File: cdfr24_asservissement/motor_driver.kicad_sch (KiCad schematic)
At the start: 14 parts

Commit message: Place components
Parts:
- renumbered C26 to C19, CR1 to CR2, C27 to Cen2, R11 to R14, R21 to R15, R22 to R16
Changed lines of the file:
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@@
 		(dnp no)
 		(fields_autoplaced yes)
-		(property "Reference" "#PWR022"
+		(property "Reference" "#PWR067"
 			(at 233.68 68.58 0)
 			(effects
@@
 			(project "cdfr24_asservissement"
 				(path "/c6b82269-16f5-49e6-8b51-4d12a40a3077/084e419c-7880-44c5-a0d2-721d5e789f19"
-					(reference "#PWR022")
-					(unit 1)
-				)
-				(path "/c6b82269-16f5-49e6-8b51-4d12a40a3077/fbaa2c7d-8eee-479f-b1be-bb54414743c2"
-					(reference "#PWR016")
+					(reference "#PWR067")
+					(unit 1)
+				)
+				(path "/c6b82269-16f5-49e6-8b51-4d12a40a3077/fbaa2c7d-8eee-479f-b1be-bb54414743c2"
+					(reference "#PWR058")
 					(unit 1)
 				)
@@
 		(dnp no)
 		(fields_autoplaced yes)
-		(property "Reference" "#PWR052"
+		(property "Reference" "#PWR070"
 			(at 194.31 100.33 0)
 			(effects
@@
 			(project "cdfr24_asservissement"
 				(path "/c6b82269-16f5-49e6-8b51-4d12a40a3077/084e419c-7880-44c5-a0d2-721d5e789f19"
-					(reference "#PWR052")
-					(unit 1)
-				)
-				(path "/c6b82269-16f5-49e6-8b51-4d12a40a3077/fbaa2c7d-8eee-479f-b1be-bb54414743c2"
-					(reference "#PWR046")
+					(reference "#PWR070")
+					(unit 1)
+				)
+				(path "/c6b82269-16f5-49e6-8b51-4d12a40a3077/fbaa2c7d-8eee-479f-b1be-bb54414743c2"
+					(reference "#PWR061")
 					(unit 1)
 				)
@@
 		(dnp no)
 		(fields_autoplaced yes)
-		(property "Reference" "#PWR057"
+		(property "Reference" "#PWR068"
 			(at 107.95 93.98 0)
 			(effects
@@
 			(project "cdfr24_asservissement"
 				(path "/c6b82269-16f5-49e6-8b51-4d12a40a3077/084e419c-7880-44c5-a0d2-721d5e789f19"
-					(reference "#PWR057")
-					(unit 1)
-				)
-				(path "/c6b82269-16f5-49e6-8b51-4d12a40a3077/fbaa2c7d-8eee-479f-b1be-bb54414743c2"
-					(reference "#PWR044")
+					(reference "#PWR068")
+					(unit 1)
+				)
+				(path "/c6b82269-16f5-49e6-8b51-4d12a40a3077/fbaa2c7d-8eee-479f-b1be-bb54414743c2"
+					(reference "#PWR059")
 					(unit 1)
 				)
@@
 		(on_board yes)
 		(dnp no)
-		(property "Reference" "R21"
+		(property "Reference" "R15"
 			(at 124.46 96.647 90)
 			(effects
@@
 			(project "cdfr24_asservissement"
 				(path "/c6b82269-16f5-49e6-8b51-4d12a40a3077/084e419c-7880-44c5-a0d2-721d5e789f19"
-					(reference "R21")
+					(reference "R15")
 					(unit 1)
 				)
@@
 		(dnp no)
 		(fields_autoplaced yes)
-		(property "Reference" "R22"
+		(property "Reference" "R16"
 			(at 197.104 102.87 0)
 			(effects
@@
 			(project "cdfr24_asservissement"
 				(path "/c6b82269-16f5-49e6-8b51-4d12a40a3077/084e419c-7880-44c5-a0d2-721d5e789f19"
-					(reference "R22")
-					(unit 1)
-				)
-				(path "/c6b82269-16f5-49e6-8b51-4d12a40a3077/fbaa2c7d-8eee-479f-b1be-bb54414743c2"
-					(reference "R20")
+					(reference "R16")
+					(unit 1)
+				)
+				(path "/c6b82269-16f5-49e6-8b51-4d12a40a3077/fbaa2c7d-8eee-479f-b1be-bb54414743c2"
+					(reference "R13")
 					(unit 1)
 				)
@@
 		(on_board yes)
 		(dnp no)
-		(property "Reference" "#PWR058"
+		(property "Reference" "#PWR069"
 			(at 124.46 83.82 0)
 			(effects
@@
 			(project "cdfr24_asservissement"
 				(path "/c6b82269-16f5-49e6-8b51-4d12a40a3077/084e419c-7880-44c5-a0d2-721d5e789f19"
-					(reference "#PWR058")
-					(unit 1)
-				)
-				(path "/c6b82269-16f5-49e6-8b51-4d12a40a3077/fbaa2c7d-8eee-479f-b1be-bb54414743c2"
-					(reference "#PWR045")
+					(reference "#PWR069")
+					(unit 1)
+				)
+				(path "/c6b82269-16f5-49e6-8b51-4d12a40a3077/fbaa2c7d-8eee-479f-b1be-bb54414743c2"
+					(reference "#PWR060")
 					(unit 1)
 				)
@@
 		(dnp no)
 		(fields_autoplaced yes)
-		(property "Reference" "R11"
+		(property "Reference" "R14"
 			(at 231.14 26.67 90)
 			(effects
@@
 			(project "cdfr24_asservissement"
 				(path "/c6b82269-16f5-49e6-8b51-4d12a40a3077/084e419c-7880-44c5-a0d2-721d5e789f19"
-					(reference "R11")
+					(reference "R14")
 					(unit 1)
 				)
@@
 		(dnp no)
 		(fields_autoplaced yes)
-		(property "Reference" "#PWR064"
+		(property "Reference" "#PWR073"
 			(at 82.55 153.67 0)
 			(effects
@@
 			(project "cdfr24_asservissement"
 				(path "/c6b82269-16f5-49e6-8b51-4d12a40a3077/084e419c-7880-44c5-a0d2-721d5e789f19"
+					(reference "#PWR073")
+					(unit 1)
+				)
+				(path "/c6b82269-16f5-49e6-8b51-4d12a40a3077/fbaa2c7d-8eee-479f-b1be-bb54414743c2"
 					(reference "#PWR064")
-					(unit 1)
-				)
-				(path "/c6b82269-16f5-49e6-8b51-4d12a40a3077/fbaa2c7d-8eee-479f-b1be-bb54414743c2"
-					(reference "#PWR049")
 					(unit 1)
 				)
@@
 		(dnp no)
 		(fields_autoplaced yes)
-		(property "Reference" "#PWR028"
+		(property "Reference" "#PWR065"
 			(at 224.79 38.1 0)
 			(effects
@@
 			(project "cdfr24_asservissement"
 				(path "/c6b82269-16f5-49e6-8b51-4d12a40a3077/084e419c-7880-44c5-a0d2-721d5e789f19"
-					(reference "#PWR028")
-					(unit 1)
-				)
-				(path "/c6b82269-16f5-49e6-8b51-4d12a40a3077/fbaa2c7d-8eee-479f-b1be-bb54414743c2"
-					(reference "#PWR025")
+					(reference "#PWR065")
+					(unit 1)
+				)
+				(path "/c6b82269-16f5-49e6-8b51-4d12a40a3077/fbaa2c7d-8eee-479f-b1be-bb54414743c2"
+					(reference "#PWR056")
 					(unit 1)
 				)
@@
 		(dnp no)
 		(fields_autoplaced yes)
-		(property "Reference" "CR1"
+		(property "Reference" "CR2"
 			(at 154.94 90.17 0)
 			(effects
@@
 		(dnp no)
 		(fields_autoplaced yes)
-		(property "Reference" "#PWR060"
+		(property "Reference" "#PWR071"
 			(at 97.79 114.3 0)
 			(effects
@@
 			(project "cdfr24_asservissement"
 				(path "/c6b82269-16f5-49e6-8b51-4d12a40a3077/084e419c-7880-44c5-a0d2-721d5e789f19"
-					(reference "#PWR060")
-					(unit 1)
-				)
-				(path "/c6b82269-16f5-49e6-8b51-4d12a40a3077/fbaa2c7d-8eee-479f-b1be-bb54414743c2"
-					(reference "#PWR047")
+					(reference "#PWR071")
+					(unit 1)
+				)
+				(path "/c6b82269-16f5-49e6-8b51-4d12a40a3077/fbaa2c7d-8eee-479f-b1be-bb54414743c2"
+					(reference "#PWR062")
 					(unit 1)
 				)
@@
 		(dnp no)
 		(fields_autoplaced yes)
-		(property "Reference" "C27"
-			(at 116.84 78.232 90)
+		(property "Reference" "Cen2"
+			(at 116.84 77.47 90)
 			(effects
 				(font
@@
 		)
 		(property "Value" "5.6n"
-			(at 116.84 80.772 90)
+			(at 116.84 80.01 90)
 			(effects
 				(font
@@
 			(project "cdfr24_asservissement"
 				(path "/c6b82269-16f5-49e6-8b51-4d12a40a3077/084e419c-7880-44c5-a0d2-721d5e789f19"
-					(reference "C27")
+					(reference "Cen2")
 					(unit 1)
 				)
@@
 		(dnp no)
 		(fields_autoplaced yes)
-		(property "Reference" "#PWR063"
+		(property "Reference" "#PWR072"
 			(at 82.55 137.16 0)
 			(effects
@@
 			(project "cdfr24_asservissement"
 				(path "/c6b82269-16f5-49e6-8b51-4d12a40a3077/084e419c-7880-44c5-a0d2-721d5e789f19"
+					(reference "#PWR072")
+					(unit 1)
+				)
+				(path "/c6b82269-16f5-49e6-8b51-4d12a40a3077/fbaa2c7d-8eee-479f-b1be-bb54414743c2"
 					(reference "#PWR063")
-					(unit 1)
-				)
-				(path "/c6b82269-16f5-49e6-8b51-4d12a40a3077/fbaa2c7d-8eee-479f-b1be-bb54414743c2"
-					(reference "#PWR048")
 					(unit 1)
 				)
@@
 		(dnp no)
 		(fields_autoplaced yes)
-		(property "Reference" "C26"
+		(property "Reference" "C19"
 			(at 221.996 53.34 0)
 			(effects
@@
 			(project "cdfr24_asservissement"
 				(path "/c6b82269-16f5-49e6-8b51-4d12a40a3077/084e419c-7880-44c5-a0d2-721d5e789f19"
-					(reference "C26")
-					(unit 1)
-				)
-				(path "/c6b82269-16f5-49e6-8b51-4d12a40a3077/fbaa2c7d-8eee-479f-b1be-bb54414743c2"
 					(reference "C19")
+					(unit 1)
+				)
+				(path "/c6b82269-16f5-49e6-8b51-4d12a40a3077/fbaa2c7d-8eee-479f-b1be-bb54414743c2"
+					(reference "C18")
 					(unit 1)
 				)
@@
 		(dnp no)
 		(fields_autoplaced yes)
-		(property "Reference" "#PWR055"
+		(property "Reference" "#PWR066"
 			(at 218.44 66.04 0)
 			(effects
@@
 			(project "cdfr24_asservissement"
 				(path "/c6b82269-16f5-49e6-8b51-4d12a40a3077/084e419c-7880-44c5-a0d2-721d5e789f19"
-					(reference "#PWR055")
-					(unit 1)
-				)
-				(path "/c6b82269-16f5-49e6-8b51-4d12a40a3077/fbaa2c7d-8eee-479f-b1be-bb54414743c2"
-					(reference "#PWR042")
+					(reference "#PWR066")
+					(unit 1)
+				)
+				(path "/c6b82269-16f5-49e6-8b51-4d12a40a3077/fbaa2c7d-8eee-479f-b1be-bb54414743c2"
+					(reference "#PWR057")
 					(unit 1)
 				)
@@
 		(dnp no)
 		(fields_autoplaced yes)
-		(property "Reference" "CR1"
+		(property "Reference" "CR2"
 			(at 274.32 52.0699 0)
 			(effects

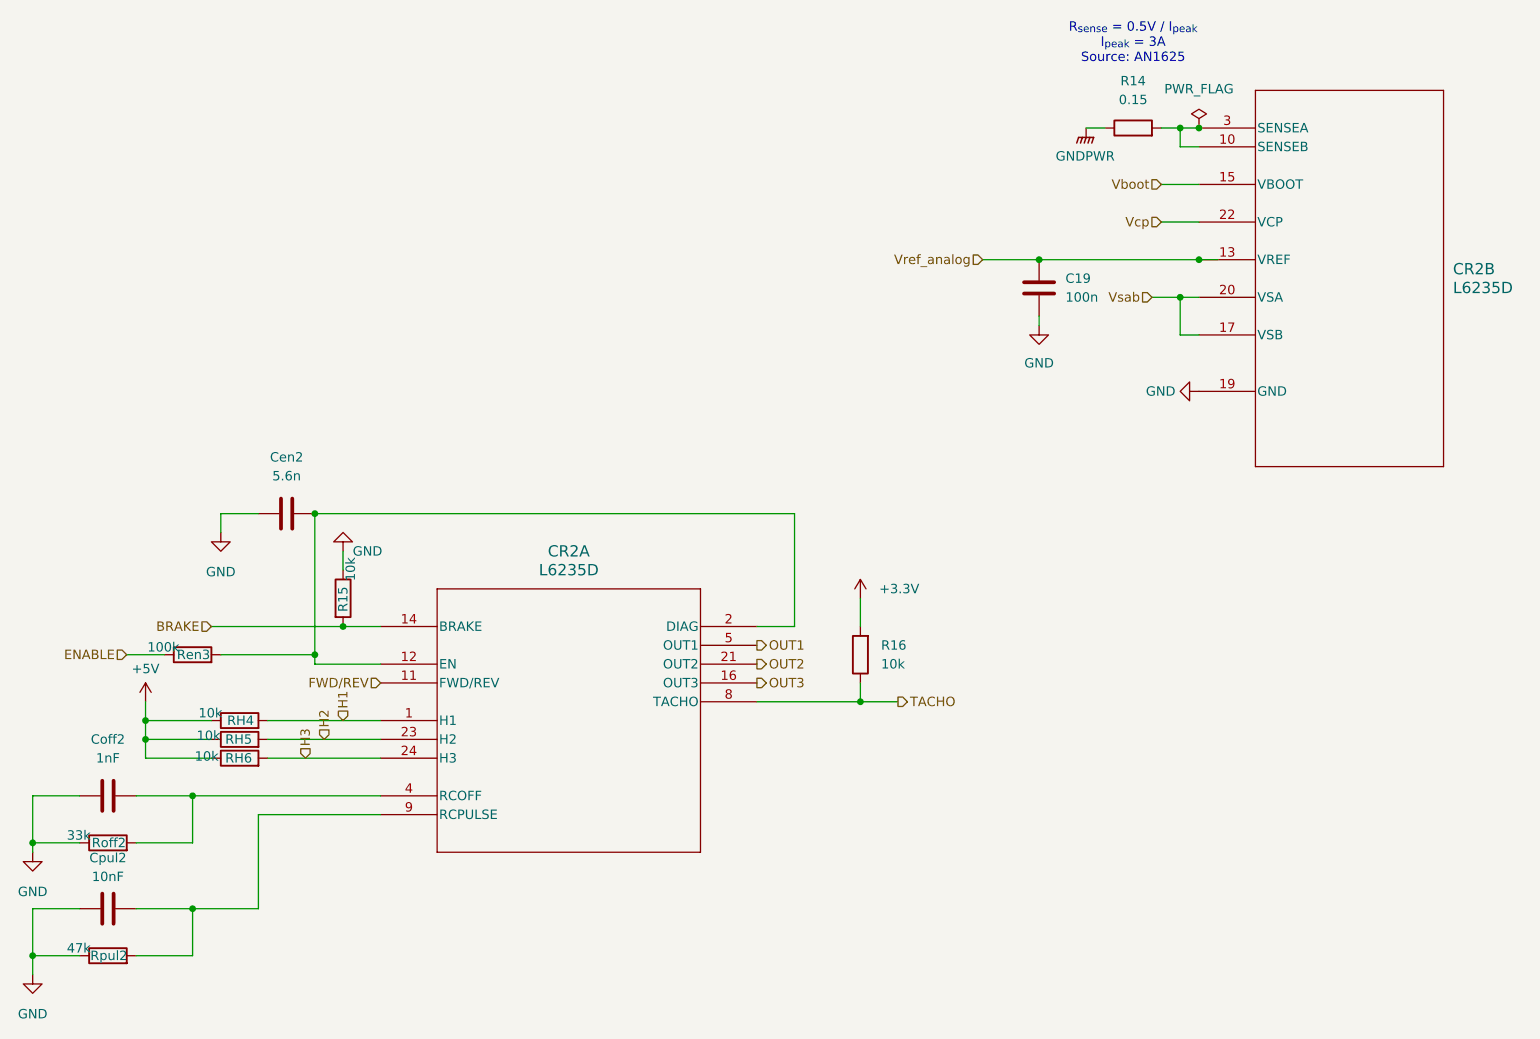
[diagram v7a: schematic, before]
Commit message: Improve placement
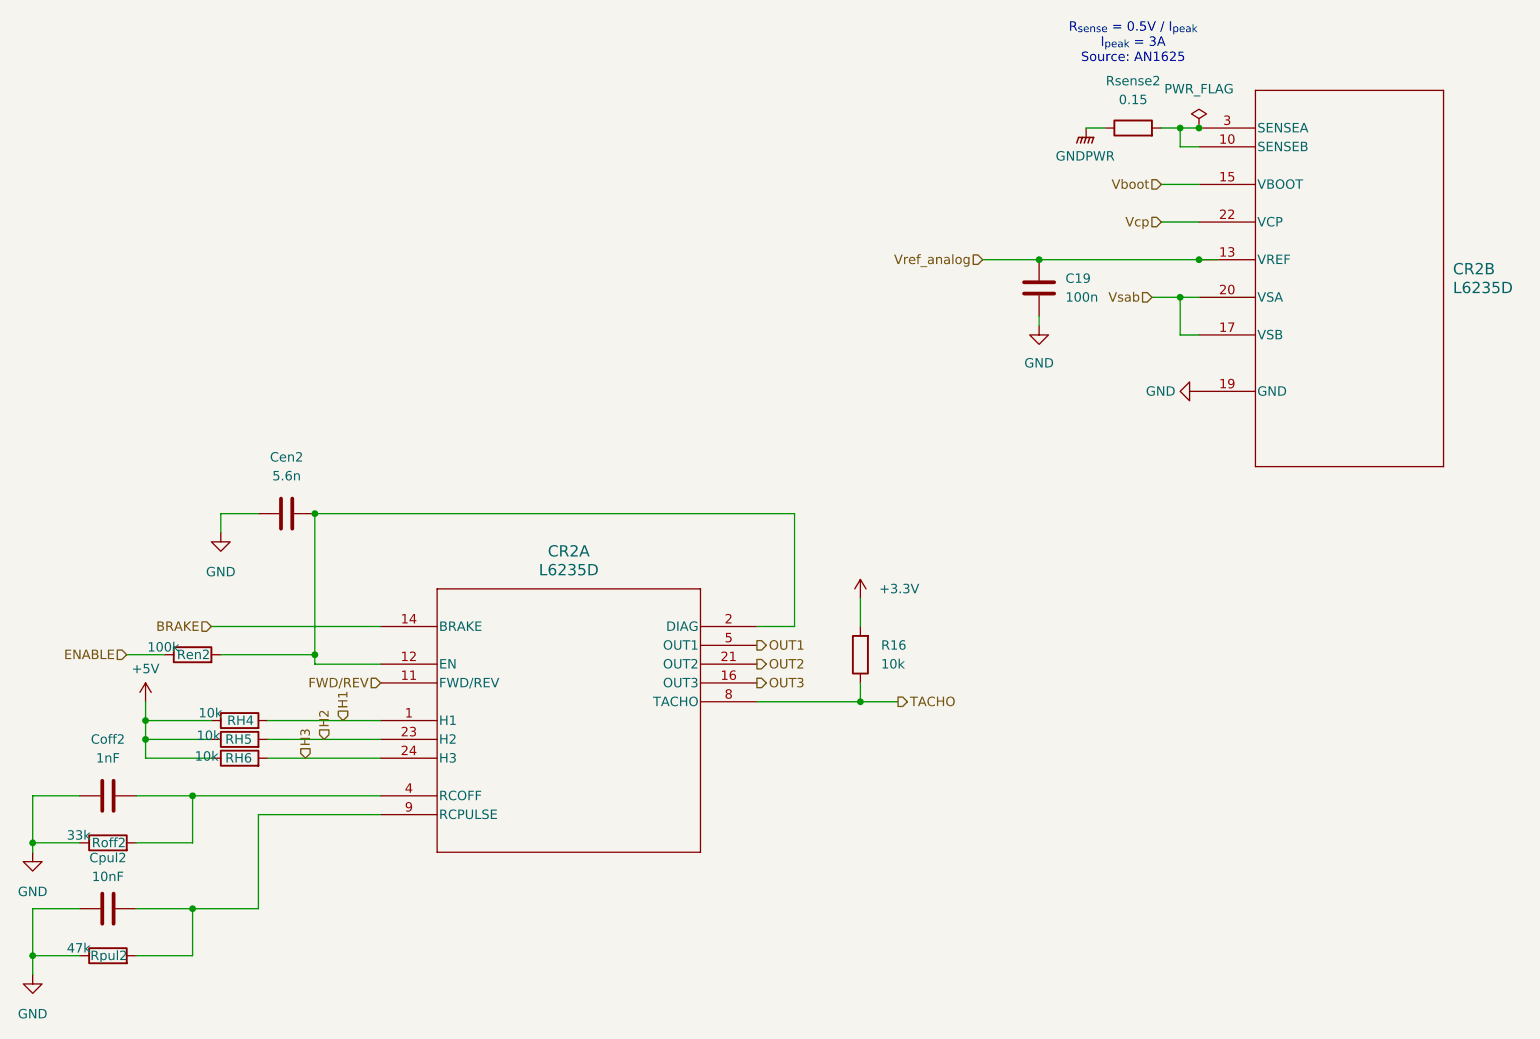
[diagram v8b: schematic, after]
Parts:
- removed R15: 10k, Resistor_SMD:R_0805_2012Metric_Pad1.20x1.40mm_HandSolder, symbol Device:R
- renumbered Ren3 to Ren2, R14 to Rsense2
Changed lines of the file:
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@@
-	)
-	(junction
-		(at 124.46 100.33)
-		(diameter 0)
-		(color 0 0 0 0)
 	)
 	(junction
@@
 	(wire
 		(pts
-			(xy 129.54 100.33) (xy 124.46 100.33)
+			(xy 106.68 100.33) (xy 129.54 100.33)
 		)
 		(stroke
@@
 	(wire
 		(pts
-			(xy 106.68 100.33) (xy 124.46 100.33)
-		)
-		(stroke
-			(width 0)
-			(type default)
-		)
-	)
-	(wire
-		(pts
 			(xy 234.95 40.64) (xy 240.03 40.64)
 		)
@@
 		(pts
 			(xy 218.44 58.42) (xy 218.44 59.69)
-		)
-		(stroke
-			(width 0)
-			(type default)
-		)
-	)
-	(wire
-		(pts
-			(xy 124.46 90.17) (xy 124.46 92.71)
 		)
 		(stroke
@@
 				)
 				(path "/c6b82269-16f5-49e6-8b51-4d12a40a3077/fbaa2c7d-8eee-479f-b1be-bb54414743c2"
-					(reference "#PWR058")
+					(reference "#PWR059")
 					(unit 1)
 				)
@@
 		(dnp no)
 		(fields_autoplaced yes)
-		(property "Reference" "#PWR070"
+		(property "Reference" "#PWR069"
 			(at 194.31 100.33 0)
 			(effects
@@
 			(project "cdfr24_asservissement"
 				(path "/c6b82269-16f5-49e6-8b51-4d12a40a3077/084e419c-7880-44c5-a0d2-721d5e789f19"
-					(reference "#PWR070")
+					(reference "#PWR069")
 					(unit 1)
 				)
@@
 				)
 				(path "/c6b82269-16f5-49e6-8b51-4d12a40a3077/fbaa2c7d-8eee-479f-b1be-bb54414743c2"
-					(reference "#PWR059")
-					(unit 1)
-				)
-			)
-		)
-	)
-	(symbol
-		(lib_id "Device:R")
-		(at 124.46 96.52 0)
-		(unit 1)
-		(exclude_from_sim no)
-		(in_bom yes)
-		(on_board yes)
-		(dnp no)
-		(property "Reference" "R15"
-			(at 124.46 96.647 90)
-			(effects
-				(font
-					(size 1.27 1.27)
-				)
-			)
-		)
-		(property "Value" "10k"
-			(at 125.476 92.583 90)
-			(effects
-				(font
-					(size 1.27 1.27)
-				)
-			)
-		)
-		(property "Footprint" "Resistor_SMD:R_0805_2012Metric_Pad1.20x1.40mm_HandSolder"
-			(at 122.682 96.52 90)
-			(effects
-				(font
-					(size 1.27 1.27)
-				)
-				(hide yes)
-			)
-		)
-		(property "Datasheet" "~"
-			(at 124.46 96.52 0)
-			(effects
-				(font
-					(size 1.27 1.27)
-				)
-				(hide yes)
-			)
-		)
-		(property "Description" ""
-			(at 124.46 96.52 0)
-			(effects
-				(font
-					(size 1.27 1.27)
-				)
-				(hide yes)
-			)
-		)
-		(pin "1"
-		)
-		(pin "2"
-		)
-		(instances
-			(project "cdfr24_asservissement"
-				(path "/c6b82269-16f5-49e6-8b51-4d12a40a3077/084e419c-7880-44c5-a0d2-721d5e789f19"
-					(reference "R15")
-					(unit 1)
-				)
-				(path "/c6b82269-16f5-49e6-8b51-4d12a40a3077/fbaa2c7d-8eee-479f-b1be-bb54414743c2"
-					(reference "Ren1")
+					(reference "#PWR060")
 					(unit 1)
 				)
@@
 		(on_board yes)
 		(dnp no)
-		(property "Reference" "Ren3"
+		(property "Reference" "Ren2"
 			(at 104.267 104.14 90)
 			(effects
@@
 			(project "cdfr24_asservissement"
 				(path "/c6b82269-16f5-49e6-8b51-4d12a40a3077/084e419c-7880-44c5-a0d2-721d5e789f19"
-					(reference "Ren3")
+					(reference "Ren2")
 					(unit 1)
 				)
 				(path "/c6b82269-16f5-49e6-8b51-4d12a40a3077/fbaa2c7d-8eee-479f-b1be-bb54414743c2"
-					(reference "Ren2")
+					(reference "Ren1")
 					(unit 1)
 				)
@@
 				)
 				(path "/c6b82269-16f5-49e6-8b51-4d12a40a3077/fbaa2c7d-8eee-479f-b1be-bb54414743c2"
-					(reference "R13")
-					(unit 1)
-				)
-			)
-		)
-	)
-	(symbol
-		(lib_id "power:GND")
-		(at 124.46 90.17 180)
-		(unit 1)
-		(exclude_from_sim no)
-		(in_bom yes)
-		(on_board yes)
-		(dnp no)
-		(property "Reference" "#PWR069"
-			(at 124.46 83.82 0)
-			(effects
-				(font
-					(size 1.27 1.27)
-				)
-				(hide yes)
-			)
-		)
-		(property "Value" "GND"
-			(at 127.762 90.17 0)
-			(effects
-				(font
-					(size 1.27 1.27)
-				)
-			)
-		)
-		(property "Footprint" ""
-			(at 124.46 90.17 0)
-			(effects
-				(font
-					(size 1.27 1.27)
-				)
-				(hide yes)
-			)
-		)
-		(property "Datasheet" ""
-			(at 124.46 90.17 0)
-			(effects
-				(font
-					(size 1.27 1.27)
-				)
-				(hide yes)
-			)
-		)
-		(property "Description" "Power symbol creates a global label with name \"GND\" , ground"
-			(at 124.46 90.17 0)
-			(effects
-				(font
-					(size 1.27 1.27)
-				)
-				(hide yes)
-			)
-		)
-		(pin "1"
-		)
-		(instances
-			(project "cdfr24_asservissement"
-				(path "/c6b82269-16f5-49e6-8b51-4d12a40a3077/084e419c-7880-44c5-a0d2-721d5e789f19"
-					(reference "#PWR069")
-					(unit 1)
-				)
-				(path "/c6b82269-16f5-49e6-8b51-4d12a40a3077/fbaa2c7d-8eee-479f-b1be-bb54414743c2"
-					(reference "#PWR060")
+					(reference "R14")
 					(unit 1)
 				)
@@
 		(dnp no)
 		(fields_autoplaced yes)
-		(property "Reference" "R14"
+		(property "Reference" "Rsense2"
 			(at 231.14 26.67 90)
 			(effects
@@
 			(project "cdfr24_asservissement"
 				(path "/c6b82269-16f5-49e6-8b51-4d12a40a3077/084e419c-7880-44c5-a0d2-721d5e789f19"
-					(reference "R14")
+					(reference "Rsense2")
 					(unit 1)
 				)
@@
 		(dnp no)
 		(fields_autoplaced yes)
-		(property "Reference" "#PWR073"
+		(property "Reference" "#PWR072"
 			(at 82.55 153.67 0)
 			(effects
@@
 			(project "cdfr24_asservissement"
 				(path "/c6b82269-16f5-49e6-8b51-4d12a40a3077/084e419c-7880-44c5-a0d2-721d5e789f19"
-					(reference "#PWR073")
+					(reference "#PWR072")
 					(unit 1)
 				)
@@
 				)
 				(path "/c6b82269-16f5-49e6-8b51-4d12a40a3077/fbaa2c7d-8eee-479f-b1be-bb54414743c2"
-					(reference "#PWR056")
+					(reference "#PWR057")
 					(unit 1)
 				)
@@
 		(dnp no)
 		(fields_autoplaced yes)
-		(property "Reference" "#PWR071"
+		(property "Reference" "#PWR070"
 			(at 97.79 114.3 0)
 			(effects
@@
 			(project "cdfr24_asservissement"
 				(path "/c6b82269-16f5-49e6-8b51-4d12a40a3077/084e419c-7880-44c5-a0d2-721d5e789f19"
-					(reference "#PWR071")
+					(reference "#PWR070")
 					(unit 1)
 				)
@@
 		(dnp no)
 		(fields_autoplaced yes)
-		(property "Reference" "#PWR072"
+		(property "Reference" "#PWR071"
 			(at 82.55 137.16 0)
 			(effects
@@
 			(project "cdfr24_asservissement"
 				(path "/c6b82269-16f5-49e6-8b51-4d12a40a3077/084e419c-7880-44c5-a0d2-721d5e789f19"
-					(reference "#PWR072")
+					(reference "#PWR071")
 					(unit 1)
 				)
@@
 				)
 				(path "/c6b82269-16f5-49e6-8b51-4d12a40a3077/fbaa2c7d-8eee-479f-b1be-bb54414743c2"
-					(reference "#PWR057")
-					(unit 1)
-				)
+					(reference "#PWR058")
+					(unit 1)
+				)
